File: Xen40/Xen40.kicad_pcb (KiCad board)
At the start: 2 copper layers, 228.6 x 95.3 mm, 120 parts, among them J1 USB SMD Header, J2 BLE TH Header, J3 OLED Header, J4 BATT Header, SW1 SW_Push, U1 ATmega32U4-AU, U2 SPX3819M5-L-3-3, U3 MCP73831-2-OT, Y1 16MHz

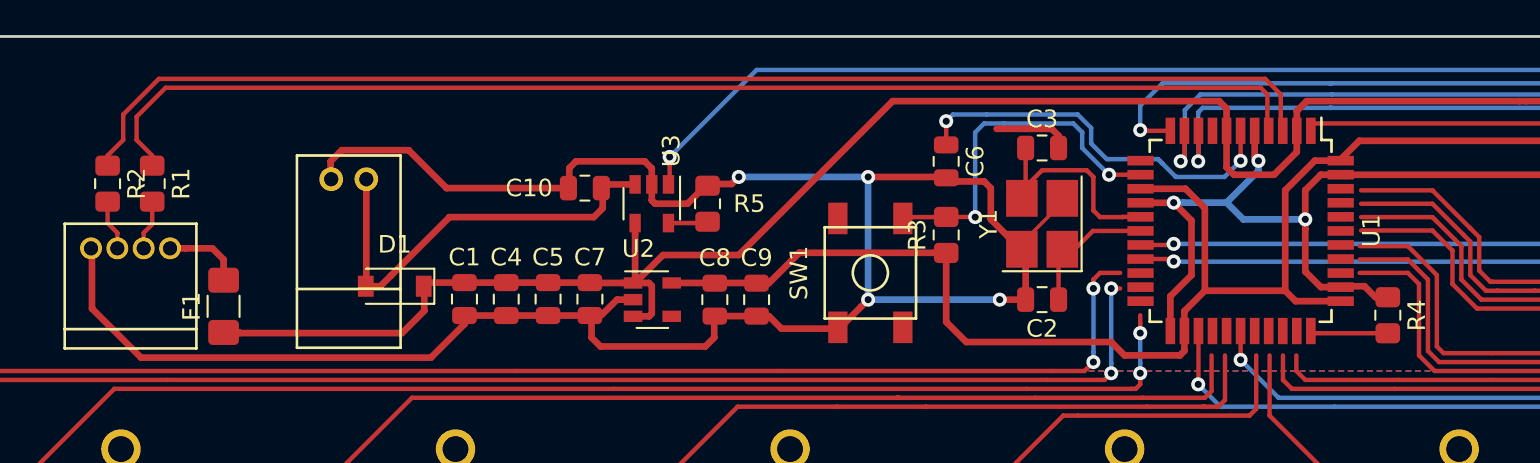
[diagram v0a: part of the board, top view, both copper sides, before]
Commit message: Finished Initial Routing for V1
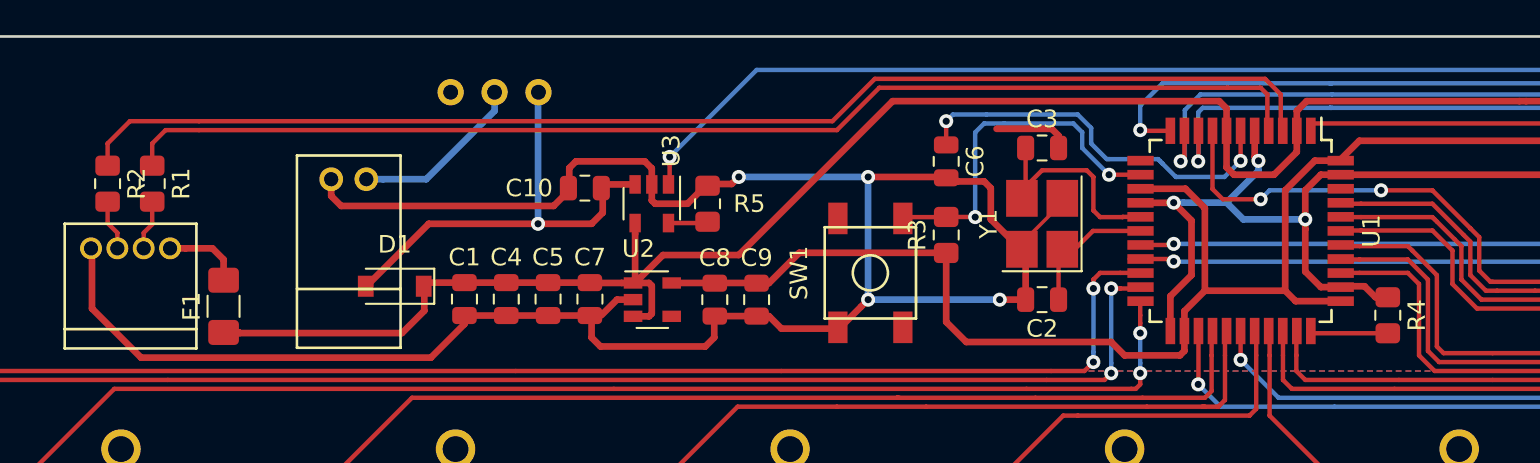
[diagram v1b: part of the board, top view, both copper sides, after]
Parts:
- added SW2: SW_SPDT, random-keyboard-parts:Batt_SW, B.Cu at (103.2, 47.6)
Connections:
- C10 pad 2: +BATT -> +VSW
- D1 pad 2: +BATT -> +VSW
- U1 pad 20: Net-(U1-Pad20) -> Col1
- U1 pad 21: Net-(U1-Pad21) -> Col2
- U1 pad 22: Net-(U1-Pad22) -> Col3
- U1 pad 26: Net-(U1-Pad26) -> Col4
- U1 pad 27: Net-(U1-Pad27) -> Col5
- U1 pad 29: Net-(U1-Pad29) -> Col6
- U1 pad 30: Net-(U1-Pad30) -> Col7
- U1 pad 31: Net-(U1-Pad31) -> Col8
- U1 pad 32: Net-(U1-Pad32) -> Col9
- U1 pad 36: Net-(U1-Pad36) -> Col10
- U1 pad 37: Net-(U1-Pad37) -> Col11
- U1 pad 38: Net-(U1-Pad38) -> Col12
- U1 pad 39: Net-(U1-Pad39) -> Row1
- U1 pad 40: Net-(U1-Pad40) -> Row2
- U1 pad 41: Net-(U1-Pad41) -> Row3
- U1 pad 8: Net-(U1-Pad8) -> Row4
- U3 pad 3: +BATT -> +VSW
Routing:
- net +VSW: track 0.00 -> 26.3 mm, vias 0 -> 1
- net +BATT: track 24.6 -> 9.98 mm
- net Row4: track 409.7 -> 421.9 mm, vias 1 -> 3
- net Net-(R1-Pad1): track 71.1 -> 68.8 mm
- net Col9: track 83.6 -> 84.8 mm
- net Col2: track 151.7 -> 153.0 mm
- net Col5: track 144.1 -> 145.3 mm
- net Col4: track 143.5 -> 144.7 mm
- net Col1: track 168.5 -> 169.6 mm
- net Row1: track 356.8 -> 357.9 mm
- net Col12: track 141.9 -> 143.0 mm
- net Col11: track 122.2 -> 123.2 mm
- net Row3: track 397.7 -> 398.7 mm
- net Row2: track 377.0 -> 378.1 mm
- net Col8: track 152.1 -> 153.1 mm
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
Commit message: Changed Location of Switch, Added Silkscreen
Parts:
- added G***: LOGO, random-keyboard-parts:sth_logo, F.Cu at (40.6, 57.4)
- moved SW2 28.6 mm to (74.6, 47.6)
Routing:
- net +VSW: track 26.3 -> 50.4 mm
- net GND: track 254.5 -> 270.2 mm
- net +BATT: track 9.98 -> 23.4 mm
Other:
- board text added: "OFF"
- board text added: "ON"
- board text added: "Prototype"
- board text added: "Xen40 v1"
